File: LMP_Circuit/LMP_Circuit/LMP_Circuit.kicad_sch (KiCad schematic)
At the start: 0 parts

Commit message: ADC, MCU, and Driver Added
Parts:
- added A1: RaspberryPi_Pico, Module:RaspberryPi_Pico_Common_Unspecified, symbol MCU_Module:RaspberryPi_Pico
- added A2: Pololu_Breakout_A4988, Module:Pololu_Breakout-16_15.2x20.3mm, symbol Driver_Motor:Pololu_Breakout_A4988
- added U1: ~, External/Custom Parts:ADS1256, symbol ADS1256_Module:ADS1256
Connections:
- new net +5V: A1.40 (VBUS), U1.1 (5V)
- new net CS: A1.10 (GPIO7), U1.7 (CS)
- new net GND: A1.13 (GND), A1.18 (GND), A1.23 (GND), A1.28 (GND), A1.3 (GND), A1.33 (AGND), A1.38 (GND), A1.8 (GND), U1.2 (GND)
- new net MISO: A1.9 (GPIO6), U1.5 (DOUT)
- new net MOSI: A1.7 (GPIO5), U1.4 (DIN)
- new net SCLK: A1.6 (GPIO4), U1.3 (SCLK)
- no-connect marks 0 -> 3

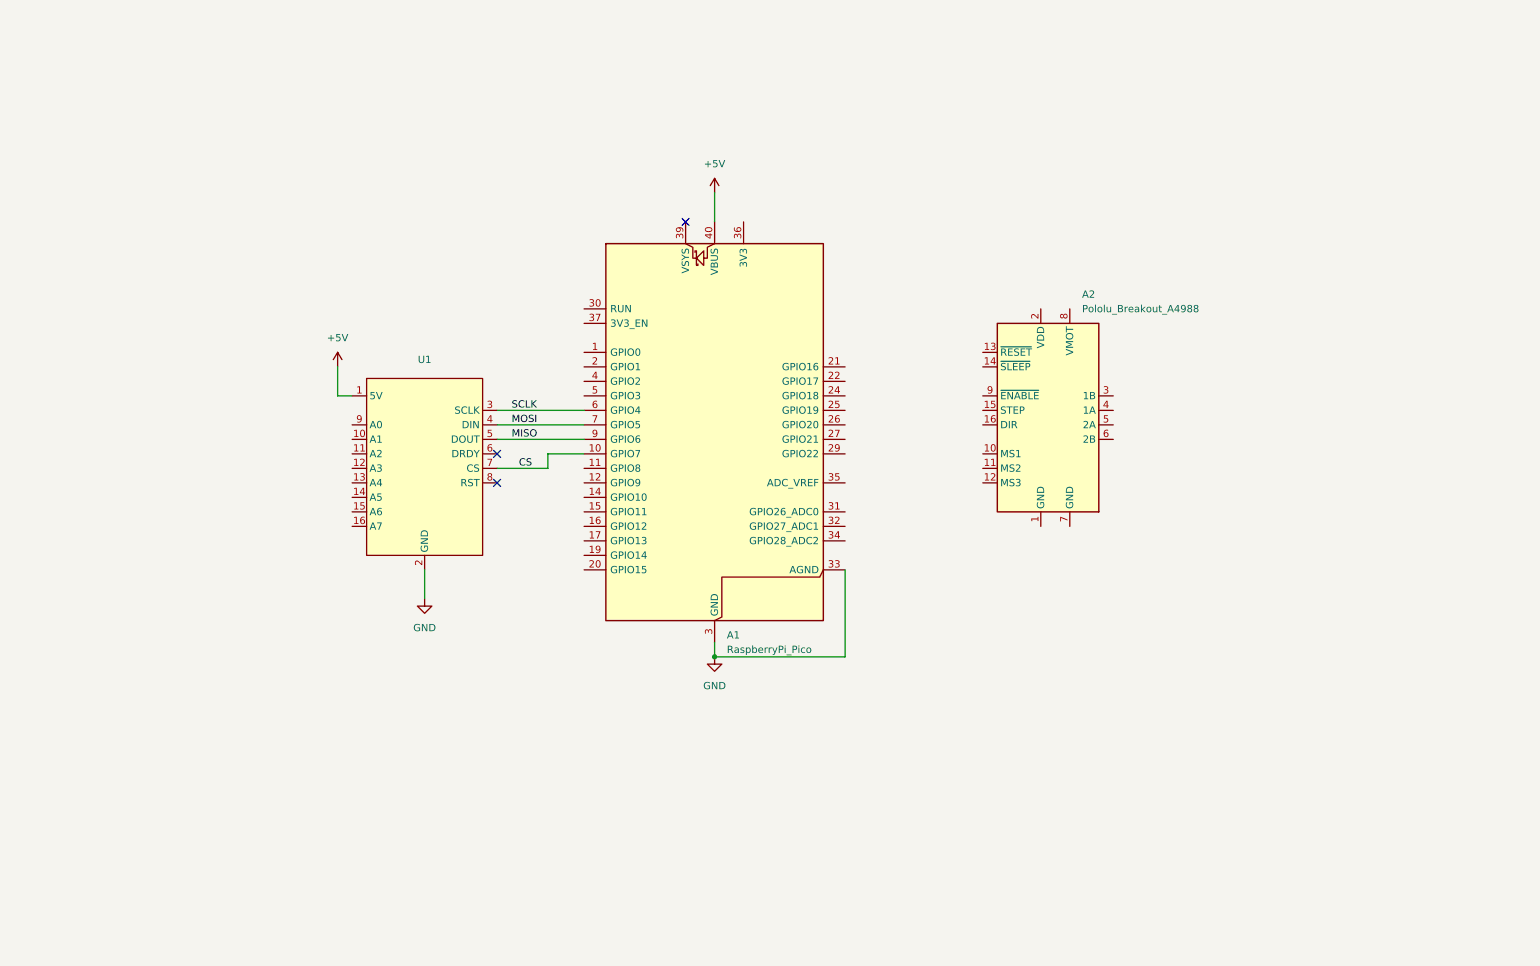
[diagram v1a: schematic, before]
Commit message: added power converter diagram and relay.
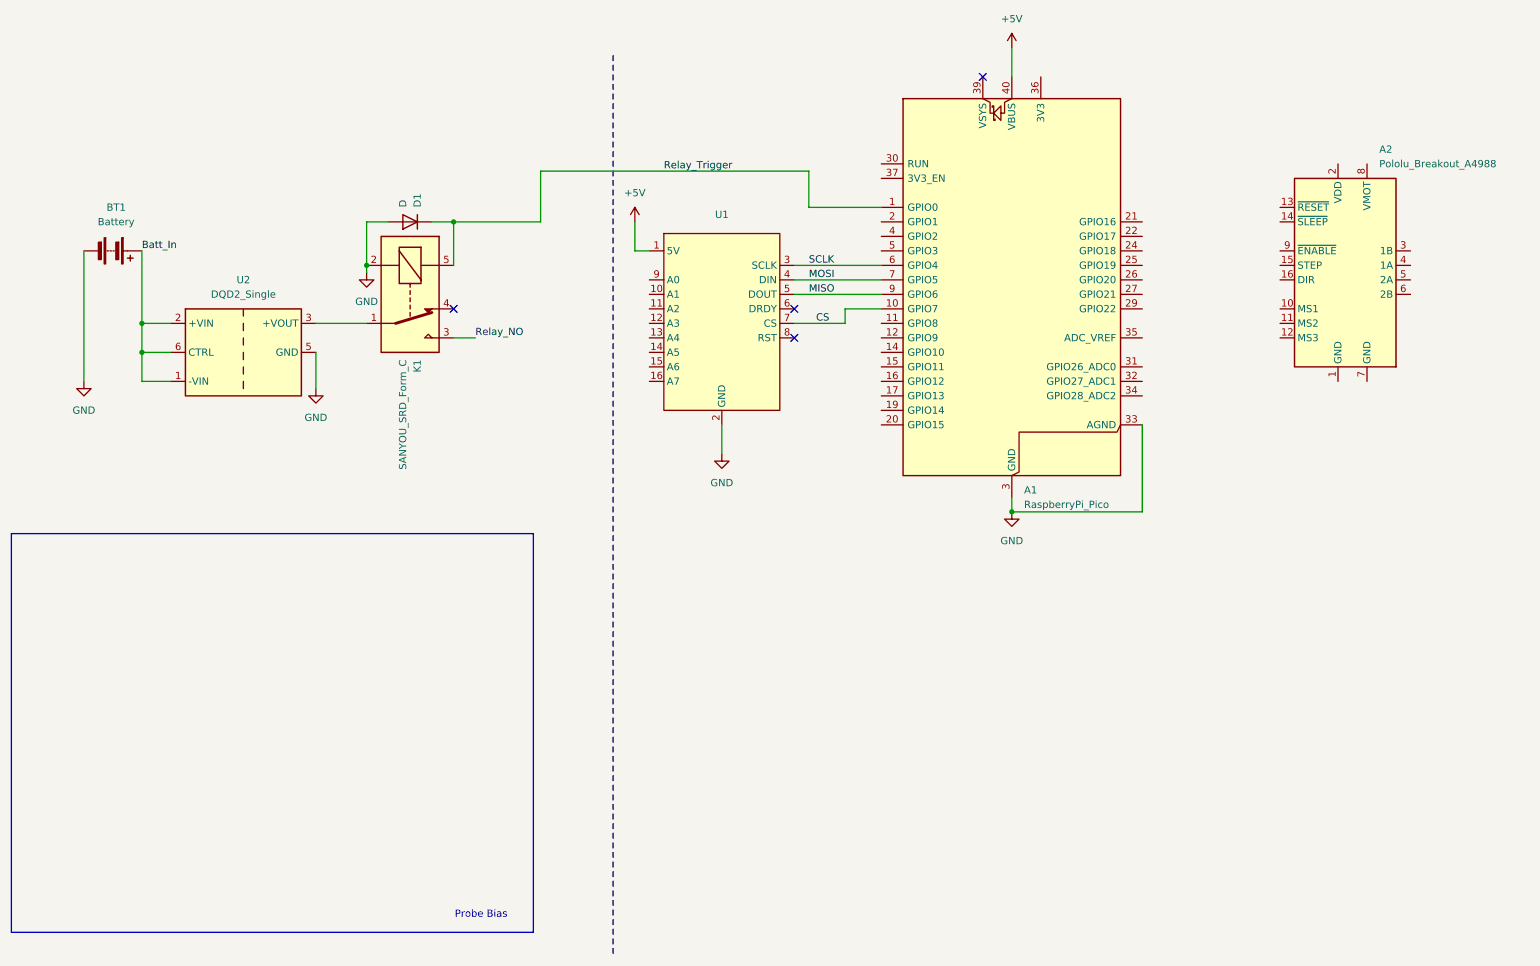
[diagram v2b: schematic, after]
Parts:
- added BT1: Battery, TerminalBlock_4Ucon:TerminalBlock_4Ucon_1x02_P3.50mm_Horizontal, symbol Device:Battery
- added D1: D, symbol Device:D
- added K1: SANYOU_SRD_Form_C, Relay_THT:Relay_SPDT_SANYOU_SRD_Series_Form_C, symbol Relay:SANYOU_SRD_Form_C
- added U2: DQD2_Single, External/Custom Parts:DQD20, symbol DQD2_Single:DQD2_Single
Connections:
- net GND: now also BT1.2 (-), D1.2 (A), K1.2, U2.5 (GND)
- net Relay_Trigger: now reaches A1.1 (GPIO0)
- net Relay_Trigger: now also D1.1 (K), K1.5
- new net: K1.1, U2.3 (+VOUT)
- new net Batt_In: BT1.1 (+), U2.1 (-VIN), U2.2 (+VIN), U2.6 (CTRL)
- new net Relay_NO: K1.3
- no-connect marks 3 -> 4
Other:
- note added: "Probe Bias"
- moved on the sheet: A1, A2, U1

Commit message: schematic near completion. Most likely functional.
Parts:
- removed A2: Pololu_Breakout_A4988, Module:Pololu_Breakout-16_15.2x20.3mm, symbol Driver_Motor:Pololu_Breakout_A4988
- removed D1: D, symbol Device:D
- removed K1: SANYOU_SRD_Form_C, Relay_THT:Relay_SPDT_SANYOU_SRD_Series_Form_C, symbol Relay:SANYOU_SRD_Form_C
- removed U1: ~, External/Custom Parts:ADS1256, symbol ADS1256_Module:ADS1256
- added A3: Pololu_Breakout_A4988, Module:Pololu_Breakout-16_15.2x20.3mm, symbol Driver_Motor:Pololu_Breakout_A4988
- added C1, C5: 100nf, Capacitor_SMD:C_0603_1608Metric, symbol Device:C
- added C2, C4, C6: 10uf, Capacitor_SMD:C_0603_1608Metric, symbol Device:C
- added C3: 100n, Capacitor_SMD:C_0603_1608Metric, symbol Device:C
- added J1: SCLK, Connector_PinHeader_1.00mm:PinHeader_1x02_P1.00mm_Vertical, symbol Connector:Conn_01x02_Socket
- added J10: RX, Connector_PinHeader_1.00mm:PinHeader_1x01_P1.00mm_Vertical, symbol Connector:Conn_01x01_Socket
- added J11: Stepper_Terminals, TerminalBlock_4Ucon:TerminalBlock_4Ucon_1x04_P3.50mm_Horizontal, symbol Connector:Screw_Terminal_01x04
- added J2: MOSI, Connector_PinHeader_1.00mm:PinHeader_1x02_P1.00mm_Vertical, symbol Connector:Conn_01x02_Socket
- added J3, J4: MISO, Connector_PinHeader_1.00mm:PinHeader_1x02_P1.00mm_Vertical, symbol Connector:Conn_01x02_Socket
- added J5: Relay_Trig, Connector_PinHeader_1.00mm:PinHeader_1x01_P1.00mm_Vertical, symbol Connector:Conn_01x01_Socket
- added J6: Power Terminal, TerminalBlock_4Ucon:TerminalBlock_4Ucon_1x03_P3.50mm_Horizontal, symbol Connector:Screw_Terminal_01x03
- added J7: Electrode+, Connector_Coaxial:BNC_TEConnectivity_1478035_Horizontal, symbol Connector:Conn_Coaxial_Small
- added J8: Electrode-, Connector_Coaxial:BNC_TEConnectivity_1478035_Horizontal, symbol Connector:Conn_Coaxial_Small
- added J9: TX, Connector_PinHeader_1.00mm:PinHeader_1x01_P1.00mm_Vertical, symbol Connector:Conn_01x01_Socket
- added Q2: NMOS, symbol Simulation_SPICE:NMOS
- added R10, R11: 1k, Resistor_SMD:R_0603_1608Metric_Pad0.98x0.95mm_HandSolder, symbol Device:R
- added R3: 5M, Resistor_SMD:R_0603_1608Metric_Pad0.98x0.95mm_HandSolder, symbol Device:R
- added R5, R7: 23.57k, Resistor_SMD:R_0603_1608Metric_Pad0.98x0.95mm_HandSolder, symbol Device:R
- added R6, R8: 3.84k, Resistor_SMD:R_0603_1608Metric_Pad0.98x0.95mm_HandSolder, symbol Device:R
- added R9: 1M, Resistor_SMD:R_0603_1608Metric_Pad0.98x0.95mm_HandSolder, symbol Device:R
- added U1, U3: ISO124U/1K, External/Custom Parts:ISO124U, symbol ISO124U:ISO124U_1K
- added U4: ADS1256, External/Custom Parts:ADS1256, symbol ADS1256_Module:ADS1256
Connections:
- net +5V: now also C2.1, C3.1, J6.2 (Pin_2), U4.1 (5V)
- net Batt_In: no longer U2.1 (-VIN)
- net CS: now also J4.1 (Pin_1), J4.2 (Pin_2), U4.7 (CS)
- net GND: now also A3.1 (GND), A3.7 (GND), C2.2, C3.2, C4.2, C5.2, J6.3 (Pin_3), R6.1, R8.1, U1.14 (GND2), U1.16 (VS2-), U3.14 (GND2), U3.16 (VS2-), U4.2 (GND); no longer BT1.2 (-), U2.5 (GND)
- net MISO: now also J3.1 (Pin_1), J3.2 (Pin_2), U4.5 (DOUT)
- net MOSI: now also J2.1 (Pin_1), J2.2 (Pin_2), U4.4 (DIN)
- net Relay_Trigger: now also A1.4 (GPIO2), J5.1 (Pin_1); no longer A1.1 (GPIO0)
- net SCLK: now also J1.1 (Pin_1), J1.2 (Pin_2), U4.3 (SCLK)
- net RX: now reaches A1.2 (GPIO1)
- net RX: now also J10.1 (Pin_1)
- net PhotoMos: now reaches A1.20 (GPIO15)
- net PhotoMos: now also R11.2
- net at A1.27 (GPIO21): now also A3.15 (STEP)
- net at A1.29 (GPIO22): now also A3.16 (DIR)
- net at A1.36 (3V3): now also A3.2 (VDD)
- net Probe_28V: now reaches U2.3 (+VOUT)
- net Probe_28V: now also C1.1, R9.1, U1.1 (VS1+), U3.1 (VS1+)
- new net: A3.13 (~{RESET}), A3.14 (~{SLEEP})
- new net: A3.3 (1B), J11.1 (Pin_1)
- new net: A3.4 (1A), J11.2 (Pin_2)
- new net: A3.5 (2A), J11.3 (Pin_3)
- new net: A3.6 (2B), J11.4 (Pin_4)
- new net: Q2.1 (D), R10.2
- new net: R7.1, U3.13 (VOUT)
- new net: Q2.2 (G), R11.1
- new net: R5.1, U1.13 (VOUT)
- new net 28V: A3.8 (VMOT), C4.1, C5.1, J6.1 (Pin_1), U1.15 (VS2+), U3.15 (VS2+)
- new net Bias_Meas: R7.2, R8.2, U4.10 (A1)
- new net Bias_Sweep: C6.2, J7.1 (In), R10.1, R9.2, U3.27 (VIN)
- new net Electrode-: J8.1 (In), R3.1, U1.27 (VIN)
- new net GND1: BT1.2 (-), C1.2, C6.1, J7.2 (Ext), J8.2 (Ext), Q2.3 (S), R3.2, U1.2 (VS1-), U1.28 (GND1), U2.1 (-VIN), U2.5 (GND), U3.2 (VS1-), U3.28 (GND1)
- new net Output_Meas: R5.2, R6.2, U4.9 (A0)
- new net TX: A1.1 (GPIO0), J9.1 (Pin_1)
- no-connect marks 4 -> 1
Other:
- note added: "Electrically Isolated"
- moved on the sheet: A1, BT1, U2

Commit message: initial layout created.
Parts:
- added J12: ISO_Power_Terminal, TerminalBlock_4Ucon:TerminalBlock_4Ucon_1x02_P3.50mm_Horizontal, symbol Connector:Screw_Terminal_01x02
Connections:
- net GND1: now also J12.2 (Pin_2)
- net Probe_28V: now also J12.1 (Pin_1)
- net +3.3V: now reaches A1.36 (3V3), A3.2 (VDD)
- net 1B: now reaches A3.3 (1B), J11.1 (Pin_1)
- net 1A: now reaches A3.4 (1A), J11.2 (Pin_2)
- net 2A: now reaches A3.5 (2A), J11.3 (Pin_3)
- net 2B: now reaches A3.6 (2B), J11.4 (Pin_4)
- no-connect marks 1 -> 32

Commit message: Added Photomos. finished layout
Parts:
- removed Q2: NMOS, symbol Simulation_SPICE:NMOS
- added C7: 1uf, Capacitor_SMD:C_0603_1608Metric, symbol Device:C
- added C8: 300nf, Capacitor_SMD:C_0603_1608Metric, symbol Device:C
- added K1: AQV101AZ, SOP254P960X390-6N, symbol AQV101AZ:AQV101AZ
- added R1: 1k, Resistor_SMD:R_0603_1608Metric_Pad0.98x0.95mm_HandSolder, symbol Device:R
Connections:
- net Bias_Meas: now also C7.2
- net Electrode-: now also C8.2
- net GND: now also C7.1, K1.1 (A), R1.1
- net GND1: now also C8.1, K1.4 (OUT_1)
- net PhotoMos: now also R1.2
- net at R10.2: now also K1.6 (OUT_2)
- net at R11.1: now also K1.2 (K)
- no-connect marks 32 -> 34
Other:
- moved on the sheet: R11, R3

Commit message: finished PCB layout with Photomos
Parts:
- K1: footprint SOP254P960X390-6N -> AQV101AZ:SOP254P960X390-6N
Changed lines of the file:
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@@
 			)
 		)
-		(property "Footprint" "SOP254P960X390-6N"
+		(property "Footprint" "AQV101AZ:SOP254P960X390-6N"
 			(at 107.95 294.31 0)
 			(effects

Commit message: LMP BOM updates
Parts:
- A1, A3, BT1, J1, J10, J2, J3, J4, J5, J9: now left out of the parts list
- C3: value 100n -> 100nf
- C8: Notes (none) -> 330nf
- J7: footprint Connector_Coaxial:BNC_TEConnectivity_1478035_Horizontal -> Connector_Coaxial:SMA_Amphenol_901-143_Horizontal
- R3: Notes (none) -> Might switch with 3M
- R5, R7: Notes (none) -> 23.4 kOhms
- R6, R8: Notes (none) -> 3.83k

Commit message: sipm BOM added, files organized a bit more
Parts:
- C1, C3, C5: Manufacturer_Part_Number (none) -> CC0603KRX7R9BB104
- C2, C4, C6: Manufacturer_Part_Number (none) -> GRM188R6YA106MA73D
- C7: Manufacturer_Part_Number (none) -> UMK107AB7105KA-T
- C8: Manufacturer_Part_Number (none) -> CGA3E3X7R1H334K080AB
- J11: Manufacturer_Part_Number (none) -> 1984633
- J12: Manufacturer_Part_Number (none) -> ED555/2DS
- J6: Manufacturer_Part_Number (none) -> 1984620
- R1, R10, R11: Manufacturer_Part_Number (none) -> RMCF0603FT1K00
- R5, R7: Manufacturer_Part_Number (none) -> RN73R1JTTD2342B25
- R6, R8: Manufacturer_Part_Number (none) -> ERA-3AEB3831V
- R9: Manufacturer_Part_Number (none) -> CRCW06031M00FKEA
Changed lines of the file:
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@@
 			)
 		)
-		(property "Description" "1984620"
+		(property "Description" ""
 			(at 181.61 83.82 0)
 			(effects
@@
 			)
 		)
+		(property "Manufacturer_Part_Number" "1984620"
+			(at 181.61 83.82 0)
+			(effects
+				(font
+					(size 1.27 1.27)
+				)
+				(hide yes)
+			)
+		)
 		(pin "2"
 		)
@@
 			)
 		)
-		(property "Description" "GRM188R6YA106MA73D"
+		(property "Description" ""
 			(at 77.47 203.2 0)
 			(effects
@@
 			)
 		)
+		(property "Manufacturer_Part_Number" "GRM188R6YA106MA73D"
+			(at 77.47 203.2 0)
+			(effects
+				(font
+					(size 1.27 1.27)
+				)
+				(hide yes)
+			)
+		)
 		(pin "2"
 		)
@@
 			)
 		)
-		(property "Description" "RMCF0603FT1K00"
+		(property "Description" ""
 			(at 142.24 208.28 0)
 			(effects
@@
 			)
 		)
+		(property "Manufacturer_Part_Number" "RMCF0603FT1K00"
+			(at 142.24 208.28 0)
+			(effects
+				(font
+					(size 1.27 1.27)
+				)
+				(hide yes)
+			)
+		)
 		(pin "1"
 		)
@@
 			)
 		)
-		(property "Description" "Unpolarized capacitor"
+		(property "Description" ""
 			(at 218.44 87.63 0)
 			(effects
@@
 			)
 		)
+		(property "Manufacturer_Part_Number" "CC0603KRX7R9BB104"
+			(at 218.44 87.63 0)
+			(effects
+				(font
+					(size 1.27 1.27)
+				)
+				(hide yes)
+			)
+		)
 		(pin "2"
 		)
@@
 			)
 		)
-		(property "Description" "GRM188R6YA106MA73D"
+		(property "Description" ""
 			(at 231.14 87.63 0)
 			(effects
@@
 			)
 		)
+		(property "Manufacturer_Part_Number" "GRM188R6YA106MA73D"
+			(at 231.14 87.63 0)
+			(effects
+				(font
+					(size 1.27 1.27)
+				)
+				(hide yes)
+			)
+		)
 		(pin "2"
 		)
@@
 			)
 		)
-		(property "Description" "ED555/2DS"
+		(property "Description" ""
 			(at 62.23 152.4 0)
 			(effects
@@
 			)
 		)
+		(property "Manufacturer_Part_Number" "ED555/2DS"
+			(at 62.23 152.4 90)
+			(effects
+				(font
+					(size 1.27 1.27)
+				)
+				(hide yes)
+			)
+		)
 		(pin "1"
 		)
@@
 			)
 		)
-		(property "Description" "RMCF0603FT1K00"
+		(property "Description" ""
 			(at 92.71 196.85 0)
 			(effects
@@
 			)
 		)
+		(property "Manufacturer_Part_Number" "RMCF0603FT1K00"
+			(at 92.71 196.85 90)
+			(effects
+				(font
+					(size 1.27 1.27)
+				)
+				(hide yes)
+			)
+		)
 		(pin "1"
 		)
@@
 			)
 		)
-		(property "Description" "ERA-3AEB3831V"
+		(property "Description" ""
 			(at 198.12 140.97 0)
 			(effects
@@
 			)
 		)
+		(property "Manufacturer_Part_Number" "ERA-3AEB3831V"
+			(at 198.12 140.97 0)
+			(effects
+				(font
+					(size 1.27 1.27)
+				)
+				(hide yes)
+			)
+		)
 		(pin "1"
 		)
@@
 			)
 		)
-		(property "Description" "RN73R1JTTD2342B25"
+		(property "Description" ""
 			(at 194.31 175.26 0)
 			(effects
@@
 			)
 		)
+		(property "Manufacturer_Part_Number" "RN73R1JTTD2342B25"
+			(at 194.31 175.26 90)
+			(effects
+				(font
+					(size 1.27 1.27)
+				)
+				(hide yes)
+			)
+		)
 		(pin "1"
 		)
@@
 			)
 		)
-		(property "Description" "UMK107AB7105KA-T"
+		(property "Description" ""
 			(at 212.09 179.07 0)
 			(effects
@@
 			)
 		)
+		(property "Manufacturer_Part_Number" "UMK107AB7105KA-T"
+			(at 212.09 179.07 0)
+			(effects
+				(font
+					(size 1.27 1.27)
+				)
+				(hide yes)
+			)
+		)
 		(pin "2"
 		)
@@
 			)
 		)
-		(property "Description" "1984633"
+		(property "Description" ""
 			(at 387.35 129.54 0)
 			(effects
@@
 			)
 		)
+		(property "Manufacturer_Part_Number" "1984633"
+			(at 387.35 129.54 0)
+			(effects
+				(font
+					(size 1.27 1.27)
+				)
+				(hide yes)
+			)
+		)
 		(pin "2"
 		)
@@
 			)
 		)
-		(property "Description" "CC0603KRX7R9BB104"
+		(property "Description" ""
 			(at 242.57 87.63 0)
 			(effects
@@
 			)
 		)
+		(property "Manufacturer_Part_Number" "CC0603KRX7R9BB104"
+			(at 242.57 87.63 0)
+			(effects
+				(font
+					(size 1.27 1.27)
+				)
+				(hide yes)
+			)
+		)
 		(pin "2"
 		)
@@
 			)
 		)
-		(property "Description" "GRM188R6YA106MA73D"
+		(property "Description" ""
 			(at 205.74 87.63 0)
 			(effects
@@
 			)
 		)
+		(property "Manufacturer_Part_Number" "GRM188R6YA106MA73D"
+			(at 205.74 87.63 0)
+			(effects
+				(font
+					(size 1.27 1.27)
+				)
+				(hide yes)
+			)
+		)
 		(pin "2"
 		)
@@
 			)
 		)
-		(property "Description" "CRCW06031M00FKEA"
+		(property "Description" ""
 			(at 71.12 196.85 0)
 			(effects
@@
 			)
 		)
+		(property "Manufacturer_Part_Number" "CRCW06031M00FKEA"
+			(at 71.12 196.85 90)
+			(effects
+				(font
+					(size 1.27 1.27)
+				)
+				(hide yes)
+			)
+		)
 		(pin "1"
 		)
@@
 			)
 		)
-		(property "Description" "CC0603KRX7R9BB104"
+		(property "Description" ""
 			(at 64.77 203.2 0)
 			(effects
@@
 			)
 		)
+		(property "Manufacturer_Part_Number" "CC0603KRX7R9BB104"
+			(at 64.77 203.2 0)
+			(effects
+				(font
+					(size 1.27 1.27)
+				)
+				(hide yes)
+			)
+		)
 		(pin "2"
 		)
@@
 			)
 		)
-		(property "Description" "AQV101AZ"
+		(property "Description" ""
 			(at 134.62 199.39 0)
 			(effects
@@
 			)
 		)
-		(property "Description" "RN73R1JTTD2342B25"
+		(property "Description" ""
 			(at 193.04 137.16 0)
 			(effects
@@
 			)
 		)
+		(property "Manufacturer_Part_Number" "RN73R1JTTD2342B25"
+			(at 193.04 137.16 90)
+			(effects
+				(font
+					(size 1.27 1.27)
+				)
+				(hide yes)
+			)
+		)
 		(pin "1"
 		)
@@
 			)
 		)
-		(property "Description" "RMCF0603FT1K00"
+		(property "Description" ""
 			(at 138.43 201.93 0)
 			(effects
@@
 			)
 		)
+		(property "Manufacturer_Part_Number" "RMCF0603FT1K00"
+			(at 138.43 201.93 90)
+			(effects
+				(font
+					(size 1.27 1.27)
+				)
+				(hide yes)
+			)
+		)
 		(pin "1"
 		)
@@
 			)
 		)
-		(property "Description" "CGA3E3X7R1H334K080AB"
+		(property "Description" ""
 			(at 132.08 140.97 0)
 			(effects
@@
 			)
 		)
+		(property "Manufacturer_Part_Number" "CGA3E3X7R1H334K080AB"
+			(at 132.08 140.97 0)
+			(effects
+				(font
+					(size 1.27 1.27)
+				)
+				(hide yes)
+			)
+		)
 		(pin "2"
 		)
@@
 			)
 		)
-		(property "Description" "ERA-3AEB3831V"
+		(property "Description" ""
 			(at 199.39 179.07 0)
 			(effects
@@
 			(at 199.39 179.07 0)
 			(effects
+				(font
+					(size 1.27 1.27)
+				)
+				(hide yes)
+			)
+		)
+		(property "Manufacturer_Part_Number" "ERA-3AEB3831V"
+			(at 199.39 179.07 0)
+			(effects
